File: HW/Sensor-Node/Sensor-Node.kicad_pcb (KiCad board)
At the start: 2 copper layers, 70 x 50 mm, 75 parts, among them IC1 STM8S003F3P, J1 CONN_01X02, J2 CONN_01X04, J3 CONN_01X02, J4 CONN_01X04, J5 CONN_01X04, J6 CONN_01X04, J7 CONN_01X03, J8 CONN_01X03, M1 NRF24L01, Q1 C1815, SW1 SW_Push, U1 TP4056, U2 RT9193-33GB, U3 MAX485

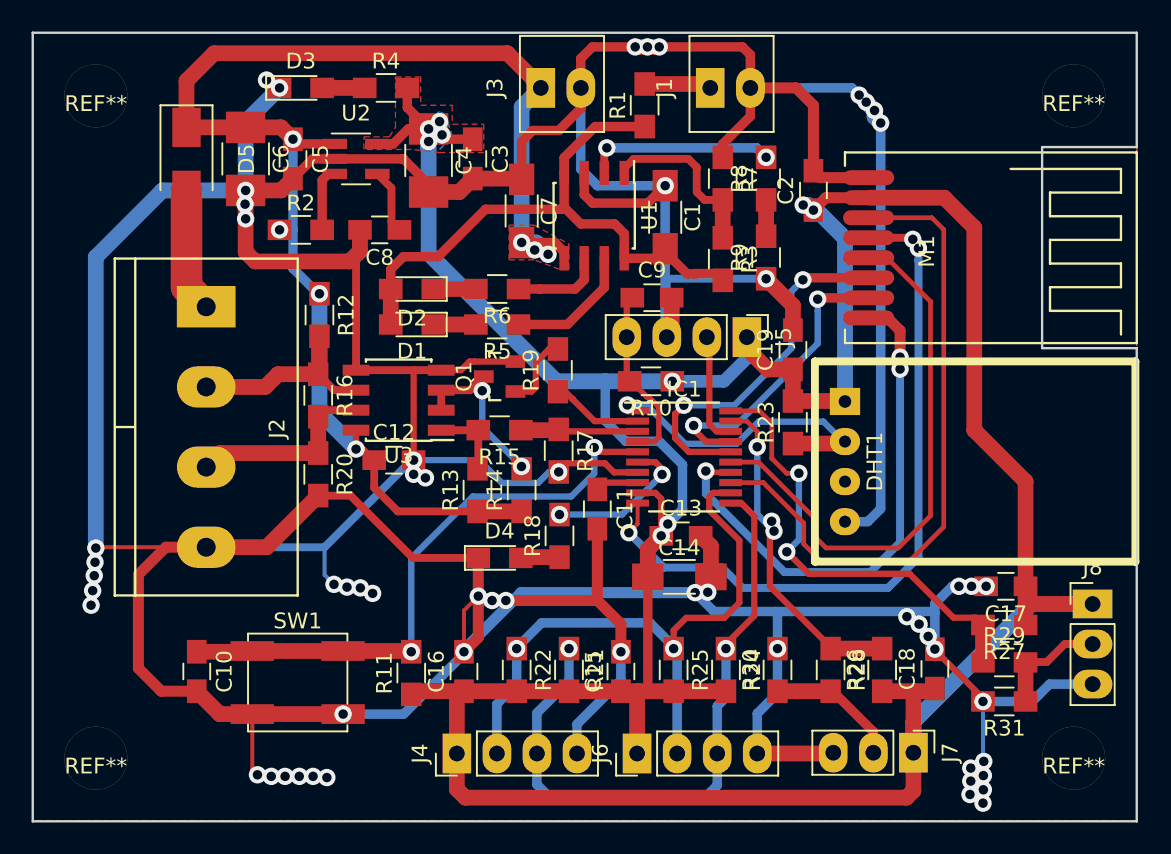
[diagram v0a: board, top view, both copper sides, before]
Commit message: modified label
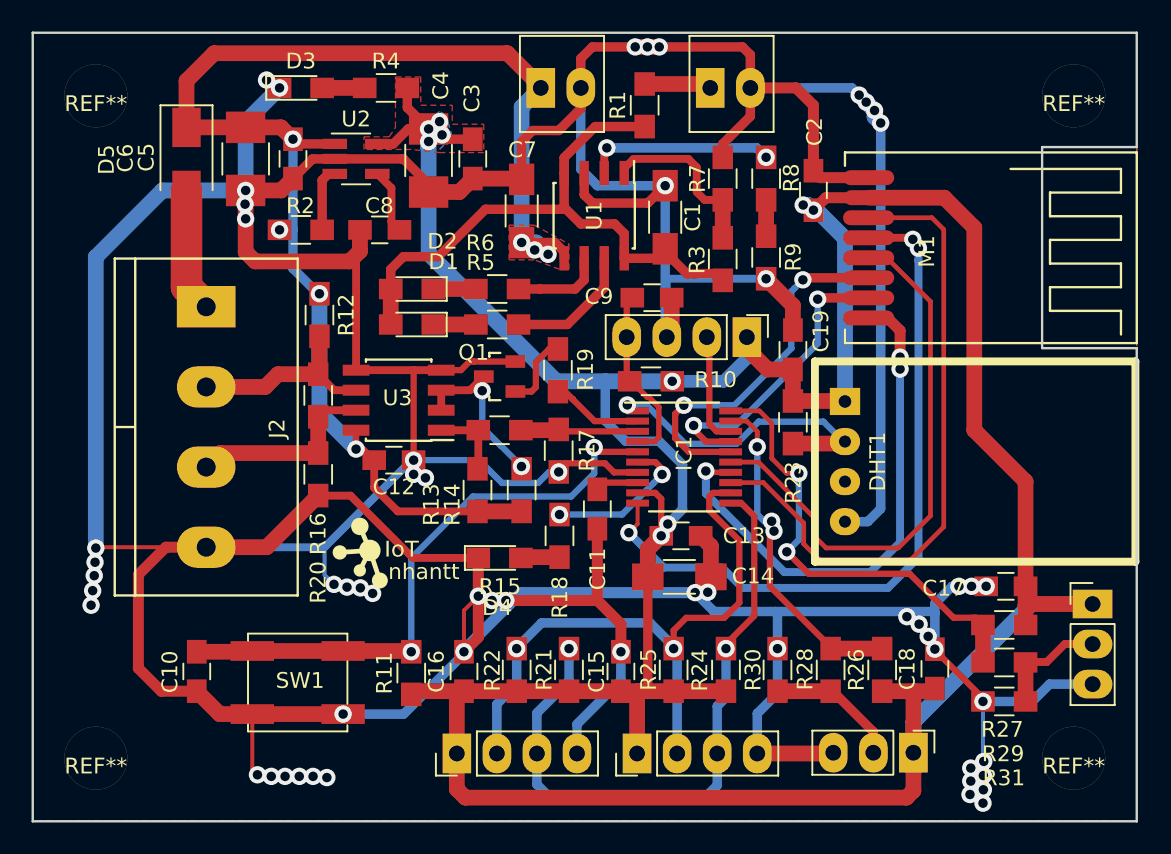
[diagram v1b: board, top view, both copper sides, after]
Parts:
- added ?: , nhantt-kicad-lib:logo2, F.Cu at (121.4, 102.8)
- renumbered J3 to BAT
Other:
- board text added: "nhantt"
